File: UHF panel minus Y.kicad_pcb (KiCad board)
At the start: 4 copper layers, 331 x 82 mm, 30 parts, among them IC1 LMT84DCKT, J1 CONSMA001-SMD-G, J2 2pin_header, J3 2pin_header, J4 2pin_header, T1 NCS1.5-232+, U1 AQZ10X, U2 S16008-33

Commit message: Added logo and name for the panel
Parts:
- added G***: LOGO, Custom-Footprints:turan-1 Logo, B.Cu at (365.0, 167.2)
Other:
- outline, holes or cut-outs redrawn
- board text added: "UHF panel Minus Y by Adkhamjonov Muhammadsolih"

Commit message: Change the small camera position
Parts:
- G***: moved to F.Cu
- moved G*** 7.35 mm to (365.0, 159.9), turned to 90 degrees
- moved U2 3.49 mm to (355.5, 140.0)
- moved R1 3.14 mm to (349.2, 148.9)
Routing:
- net SUN_-Y: track 145.7 -> 147.7 mm
- net Net-(U1-IN+(A)): track 38.1 -> 39.9 mm
- net Net-(J2-Pad2): track 20.0 -> 21.3 mm
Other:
- outline, holes or cut-outs redrawn
- board text added: "UHF panel Minus Y EM Ver 5 by Adkhamjonov Muhammadsolih"
- board text removed: "UHF panel Minus Y by Adkhamjonov Muhammadsolih"

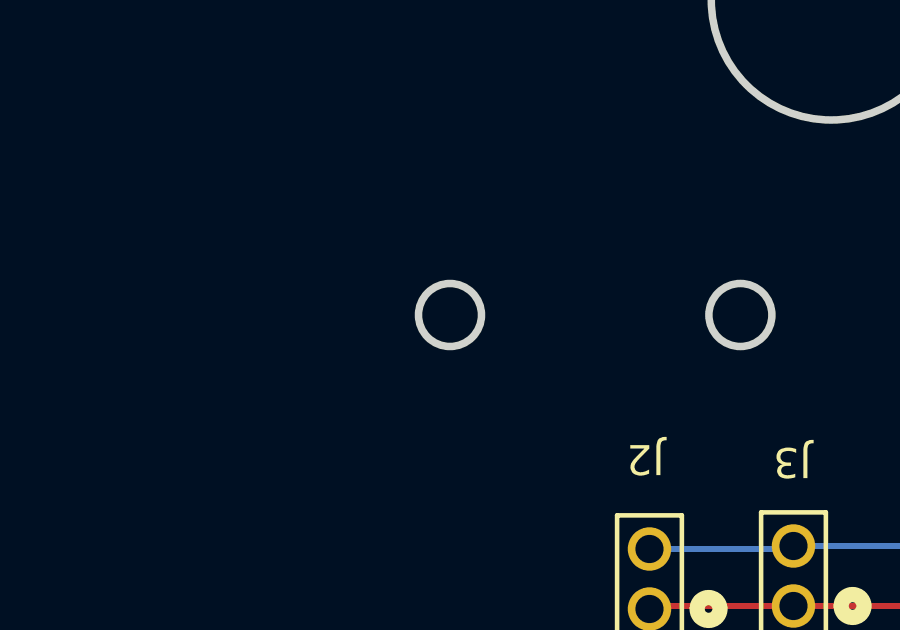
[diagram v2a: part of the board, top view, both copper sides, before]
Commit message: Added small camera
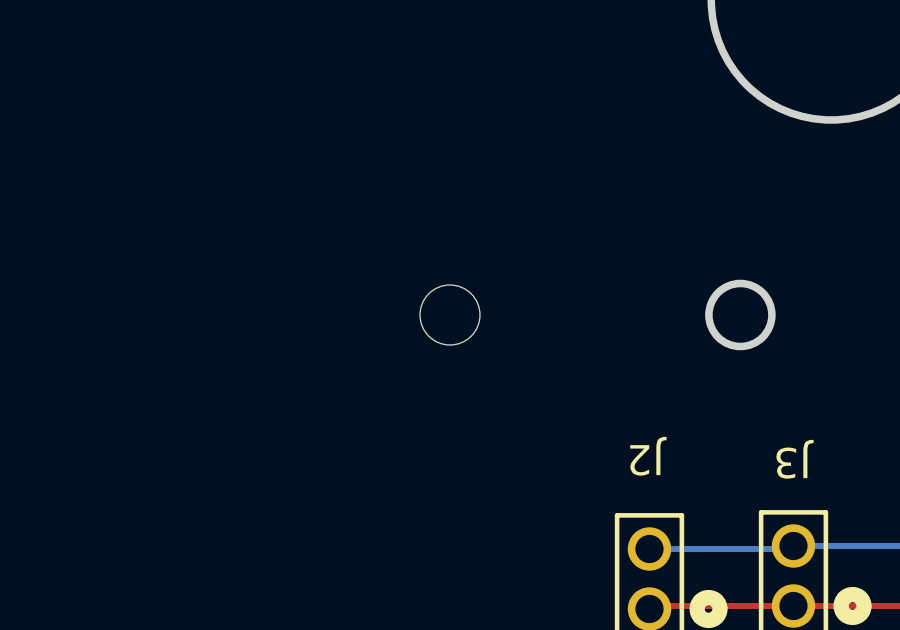
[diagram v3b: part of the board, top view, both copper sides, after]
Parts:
- added Camera: MountingHole, MountingHole:MountingHole_2.1mm, B.Cu at (329.9, 151.4)
- renumbered C3 to C1, C4 to C2, C1 to C3, C2 to C4
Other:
- outline, holes or cut-outs redrawn
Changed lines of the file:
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@@
 		(descr "Capacitor SMD 0805 (2012 Metric), square (rectangular) end terminal, IPC-7351 nominal, (Body size source: IPC-SM-782 page 76, https://www.pcb-3d.com/wordpress/wp-content/uploads/ipc-sm-782a_amendment_1_and_2.pdf, https://docs.google.com/spreadsheets/d/1BsfQQcO9C6DZCsRaXUlFlo91Tg2WpOkGARC1WS5S8t0/edit?usp=sharing), generated with kicad-footprint-generator")
 		(tags "capacitor")
-		(property "Reference" "C3"
+		(property "Reference" "C1"
 			(at 0 1.68 90)
 			(layer "B.SilkS")
@@
 		(descr "Capacitor SMD 0603 (1608 Metric), square (rectangular) end terminal, IPC-7351 nominal, (Body size source: IPC-SM-782 page 76, https://www.pcb-3d.com/wordpress/wp-content/uploads/ipc-sm-782a_amendment_1_and_2.pdf), generated with kicad-footprint-generator")
 		(tags "capacitor")
-		(property "Reference" "C1"
+		(property "Reference" "C3"
 			(at 0.367827 -1.536882 25)
 			(layer "B.SilkS")
@@
 		(descr "Capacitor SMD 0805 (2012 Metric), square (rectangular) end terminal, IPC-7351 nominal, (Body size source: IPC-SM-782 page 76, https://www.pcb-3d.com/wordpress/wp-content/uploads/ipc-sm-782a_amendment_1_and_2.pdf, https://docs.google.com/spreadsheets/d/1BsfQQcO9C6DZCsRaXUlFlo91Tg2WpOkGARC1WS5S8t0/edit?usp=sharing), generated with kicad-footprint-generator")
 		(tags "capacitor")
-		(property "Reference" "C4"
+		(property "Reference" "C2"
 			(at 0 1.68 0)
 			(layer "B.SilkS")
@@
 		(descr "Capacitor SMD 0603 (1608 Metric), square (rectangular) end terminal, IPC-7351 nominal, (Body size source: IPC-SM-782 page 76, https://www.pcb-3d.com/wordpress/wp-content/uploads/ipc-sm-782a_amendment_1_and_2.pdf), generated with kicad-footprint-generator")
 		(tags "capacitor")
-		(property "Reference" "C2"
+		(property "Reference" "C4"
 			(at -0.459206 1.486718 160)
 			(layer "B.SilkS")
@@
 		(embedded_fonts no)
 	)
+	(footprint "MountingHole:MountingHole_2.1mm"
+		(layer "B.Cu")
+		(at 329.87 151.36 180)
+		(descr "Mounting Hole 2.1mm, no annular, generated by kicad-footprint-generator mountinghole.py")
+		(tags "mountinghole")
+		(property "Reference" "Camera"
+			(at 1.49 10.7 270)
+			(layer "B.SilkS")
+			(effects
+				(font
+					(size 1 1)
+					(thickness 0.15)
+				)
+				(justify mirror)
+			)
+		)
+		(property "Value" "MountingHole"
+			(at 0.092189 -4.5 0)
+			(layer "B.Fab")
+			(effects
+				(font
+					(size 1 1)
+					(thickness 0.15)
+				)
+				(justify mirror)
+			)
+		)
+		(property "Datasheet" "~"
+			(at 0 0 0)
+			(layer "B.Fab")
+			(hide yes)
+			(effects
+				(font
+					(size 1.27 1.27)
+					(thickness 0.15)
+				)
+				(justify mirror)
+			)
+		)
+		(property "Description" "Mounting Hole without connection"
+			(at 0 0 0)
+			(layer "B.Fab")
+			(hide yes)
+			(effects
+				(font
+					(size 1.27 1.27)
+					(thickness 0.15)
+				)
+				(justify mirror)
+			)
+		)
+		(property ki_fp_filters "MountingHole*")
+		(sheetname "/")
+		(sheetfile "UHF panel minus Y.kicad_sch")
+		(attr exclude_from_pos_files exclude_from_bom)
+		(fp_circle
+			(center 0 0)
+			(end 2.1 0)
+			(stroke
+				(width 0.15)
+				(type solid)
+			)
+			(fill no)
+			(layer "Cmts.User")
+		)
+		(fp_circle
+			(center 0 0)
+			(end 2.35 0)
+			(stroke
+				(width 0.05)
+				(type solid)
+			)
+			(fill no)
+			(layer "B.CrtYd")
+		)
+		(pad "" np_thru_hole circle
+			(at 0 0 180)
+			(size 2 2)
+			(drill 2)
+			(layers "*.Cu" "*.Mask")
+		)
+		(embedded_fonts no)
+		(model "${KIPRJMOD}/KiCad-Libraries/3Ds/small camera.STEP"
+			(offset
+				(xyz 372.5 131.2 -184)
+			)
+			(scale
+				(xyz 1 1 1)
+			)
+			(rotate
+				(xyz -90 -0 90)
+			)
+		)
+	)
 	(footprint "Custom-Footprints:RESC1005X35N"
 		(layer "B.Cu")
@@
 	)
 	(gr_circle
-		(center 329.87 151.36)
-		(end 329.87 150.31)
-		(stroke
-			(width 0.25)
-			(type default)
-		)
-		(fill no)
-		(locked yes)
-		(layer "Edge.Cuts")
-	)
-	(gr_circle
 		(center 139.63 101.86)
 		(end 139.63 100.81)
@@
 		(min_thickness 0.25)
 		(filled_areas_thickness no)
-		(fill
+		(fill yes
 			(thermal_gap 0.5)
 			(thermal_bridge_width 0.5)
@@
 			(tracks not_allowed)
 			(vias not_allowed)
-			(pads not_allowed)
+			(pads allowed)
 			(copperpour not_allowed)
 			(footprints allowed)
@@
 		(min_thickness 0.25)
 		(filled_areas_thickness no)
-		(fill
+		(fill yes
 			(thermal_gap 0.5)
 			(thermal_bridge_width 0.5)
@@
 		(min_thickness 0.25)
 		(filled_areas_thickness no)
-		(fill
+		(fill yes
 			(thermal_gap 0.5)
 			(thermal_bridge_width 0.5)
@@
 		(min_thickness 0.25)
 		(filled_areas_thickness no)
-		(fill
+		(fill yes
 			(thermal_gap 0.5)
 			(thermal_bridge_width 0.5)
@@
 		(min_thickness 0.25)
 		(filled_areas_thickness no)
-		(fill
+		(fill yes
 			(thermal_gap 0.5)
 			(thermal_bridge_width 0.5)
@@
 		(min_thickness 0.25)
 		(filled_areas_thickness no)
-		(fill
+		(fill yes
 			(thermal_gap 0.5)
 			(thermal_bridge_width 0.5)
@@
 		(min_thickness 0.1524)
 		(filled_areas_thickness no)
-		(fill
+		(fill yes
 			(thermal_gap 0.2026)
 			(thermal_bridge_width 0.2026)
@@
 		(min_thickness 0.25)
 		(filled_areas_thickness no)
-		(fill
+		(fill yes
 			(thermal_gap 0.5)
 			(thermal_bridge_width 0.5)
@@
 		(min_thickness 0.25)
 		(filled_areas_thickness no)
-		(fill
+		(fill yes
 			(thermal_gap 0.5)
 			(thermal_bridge_width 0.5)
@@
 		(min_thickness 0.25)
 		(filled_areas_thickness no)
-		(fill
+		(fill yes
 			(thermal_gap 0.5)
 			(thermal_bridge_width 0.5)

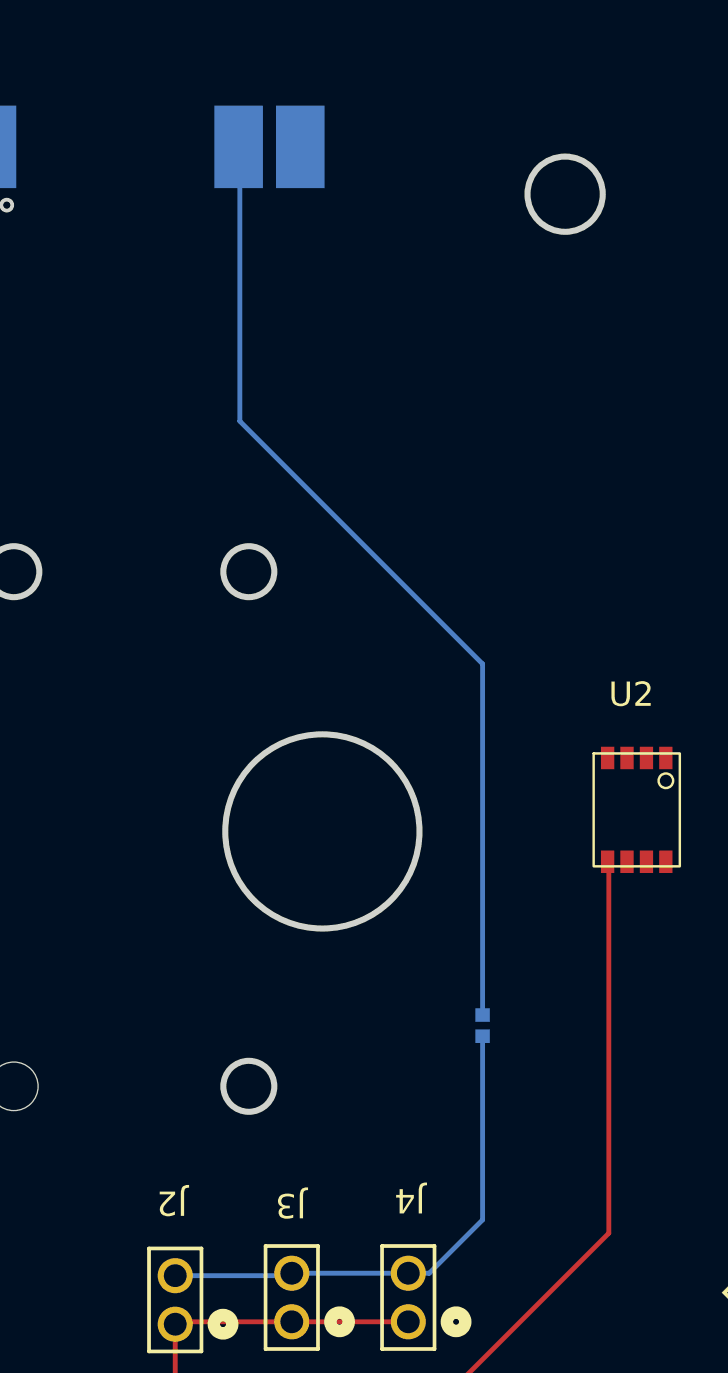
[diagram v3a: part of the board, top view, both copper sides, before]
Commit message: Add 3D for burner resistors
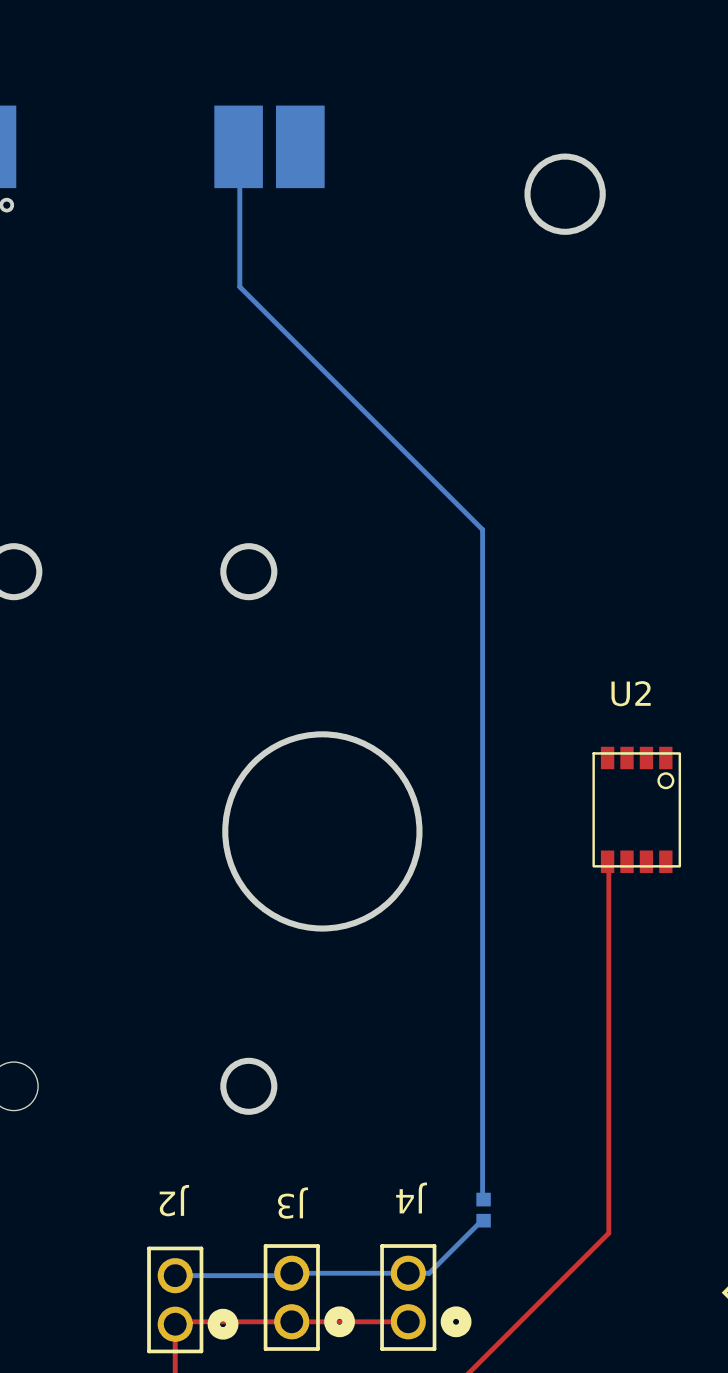
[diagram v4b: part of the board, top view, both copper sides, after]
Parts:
- moved R1 7.60 mm to (349.2, 156.5)
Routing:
- net Net-(U1-IN+(A)): track 39.9 -> 47.5 mm
- net Net-(J2-Pad2): track 21.3 -> 13.8 mm
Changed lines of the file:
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@@
 		)
 		(embedded_fonts no)
+		(model "${KIPRJMOD}/KiCad-Libraries/3Ds/R_Axial_DIN0207_L6.3mm_D2.5mm_P15.24mm_Horizontal.step"
+			(offset
+				(xyz -7.5 0 1.5)
+			)
+			(scale
+				(xyz 1 1 1)
+			)
+			(rotate
+				(xyz -0 -0 -0)
+			)
+		)
 	)
 	(footprint "Resistor_SMD:R_0805_2012Metric"
@@
 		)
 		(embedded_fonts no)
+		(model "${KIPRJMOD}/KiCad-Libraries/3Ds/R_Axial_DIN0207_L6.3mm_D2.5mm_P15.24mm_Horizontal.step"
+			(offset
+				(xyz -7.5 0 1.5)
+			)
+			(scale
+				(xyz 1 1 1)
+			)
+			(rotate
+				(xyz -0 -0 -0)
+			)
+		)
 	)
 	(footprint "Custom-Footprints:CUHS20S30,H3F"
@@
 		)
 		(embedded_fonts no)
+		(model "${KIPRJMOD}/KiCad-Libraries/3Ds/R_Axial_DIN0207_L6.3mm_D2.5mm_P15.24mm_Horizontal.step"
+			(offset
+				(xyz -7.5 0 1.5)
+			)
+			(scale
+				(xyz 1 1 1)
+			)
+			(rotate
+				(xyz -0 -0 -0)
+			)
+		)
 	)
 	(footprint "MountingHole:MountingHole_2.1mm"
@@
 	(footprint "Custom-Footprints:RESC1005X35N"
 		(layer "B.Cu")
-		(at 349.18 148.86 -90)
+		(at 349.22 156.46 -90)
 		(property "Reference" "R1"
 			(at 0.07 1.54 90)
@@
 	)
 	(segment
+		(start 346.1196 159.059999)
+		(end 346.980001 159.059999)
+		(width 0.2)
+		(layer "B.Cu")
+		(net 9)
+	)
+	(segment
+		(start 349.18 156.86)
+		(end 349.185 156.86)
+		(width 0.2)
+		(layer "B.Cu")
+		(net 9)
+	)
+	(segment
 		(start 341.3196 159.059999)
 		(end 341.28 159.020399)
@@
 	)
 	(segment
-		(start 346.1196 159.059999)
-		(end 346.980001 159.059999)
+		(start 349.185 156.86)
+		(end 349.22 156.895)
 		(width 0.2)
 		(layer "B.Cu")
@@
 	)
 	(segment
-		(start 349.18 156.86)
-		(end 349.18 149.295)
+		(start 339.18 118.43)
+		(end 339.18 112.71)
 		(width 0.2)
 		(layer "B.Cu")
-		(net 9)
+		(net 10)
 	)
 	(segment
-		(start 339.18 123.96)
-		(end 339.18 112.71)
+		(start 349.18 128.43)
+		(end 339.18 118.43)
 		(width 0.2)
 		(layer "B.Cu")
@@
 	)
 	(segment
-		(start 349.18 148.425)
-		(end 349.18 133.96)
+		(start 339.18 112.71)
+		(end 339.13 112.66)
 		(width 0.2)
 		(layer "B.Cu")
@@
 	)
 	(segment
-		(start 349.18 133.96)
-		(end 339.18 123.96)
+		(start 349.18 155.985)
+		(end 349.18 128.43)
 		(width 0.2)
 		(layer "B.Cu")
@@
 	)
 	(segment
-		(start 339.18 112.71)
-		(end 339.13 112.66)
+		(start 349.22 156.025)
+		(end 349.18 155.985)
 		(width 0.2)
 		(layer "B.Cu")
